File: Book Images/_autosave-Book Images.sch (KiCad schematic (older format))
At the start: 5 parts, among them T1 Transformer

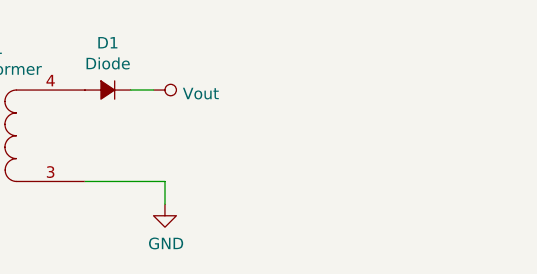
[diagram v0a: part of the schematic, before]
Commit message: adding images and rewriting intro
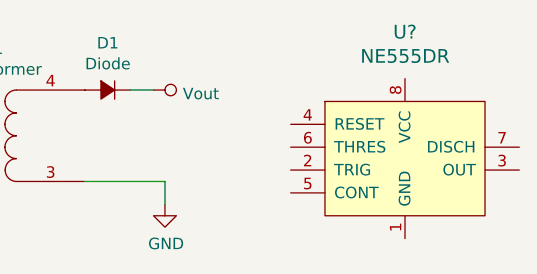
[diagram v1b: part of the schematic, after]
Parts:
- added U?: NE555DR, digikey-footprints:SOIC-8_W3.9mm, symbol dk_Clock-Timing-Programmable-Timers-and-Oscillators:NE555DR
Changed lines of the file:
@@
 Wire Wire Line
 	3350 2600 3000 2600
+$Comp
+L dk_Clock-Timing-Programmable-Timers-and-Oscillators:NE555DR U?
+U 1 1 624B1200
+P 4400 2250
+F 0 "U?" H 4400 2553 60  0000 C CNN
+F 1 "NE555DR" H 4400 2447 60  0000 C CNN
+F 2 "digikey-footprints:SOIC-8_W3.9mm" H 4600 2450 60  0001 L CNN
+F 3 "http://www.ti.com/general/docs/suppproductinfo.tsp?distId=10&gotoUrl=http%3A%2F%2Fwww.ti.com%2Flit%2Fgpn%2Fne555" H 4600 2550 60  0001 L CNN
+F 4 "296-6501-1-ND" H 4600 2650 60  0001 L CNN "Digi-Key_PN"
+F 5 "NE555DR" H 4600 2750 60  0001 L CNN "MPN"
+F 6 "Integrated Circuits (ICs)" H 4600 2850 60  0001 L CNN "Category"
+F 7 "Clock/Timing - Programmable Timers and Oscillators" H 4600 2950 60  0001 L CNN "Family"
+F 8 "http://www.ti.com/general/docs/suppproductinfo.tsp?distId=10&gotoUrl=http%3A%2F%2Fwww.ti.com%2Flit%2Fgpn%2Fne555" H 4600 3050 60  0001 L CNN "DK_Datasheet_Link"
+F 9 "/product-detail/en/texas-instruments/NE555DR/296-6501-1-ND/372490" H 4600 3150 60  0001 L CNN "DK_Detail_Page"
+F 10 "IC OSC SGL TIMER 100KHZ 8-SOIC" H 4600 3250 60  0001 L CNN "Description"
+F 11 "Texas Instruments" H 4600 3350 60  0001 L CNN "Manufacturer"
+F 12 "Active" H 4600 3450 60  0001 L CNN "Status"
+	1    4400 2250
+	1    0    0    -1
+$EndComp
 $EndSCHEMATC

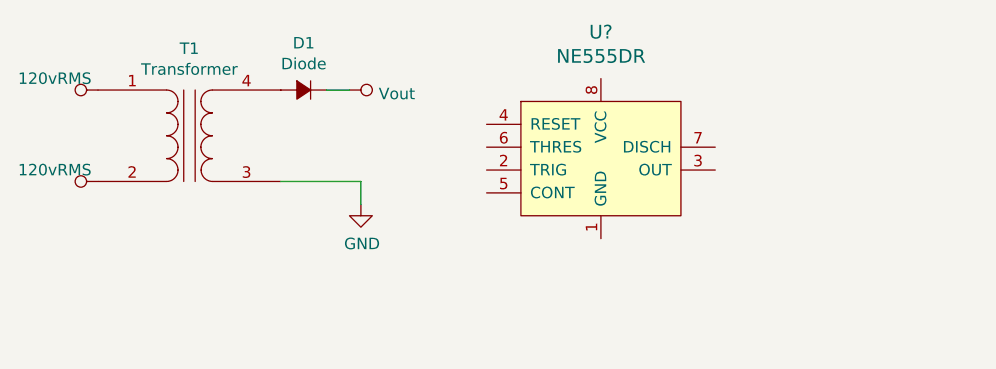
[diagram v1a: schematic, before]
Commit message: updated formating and added unregulated section
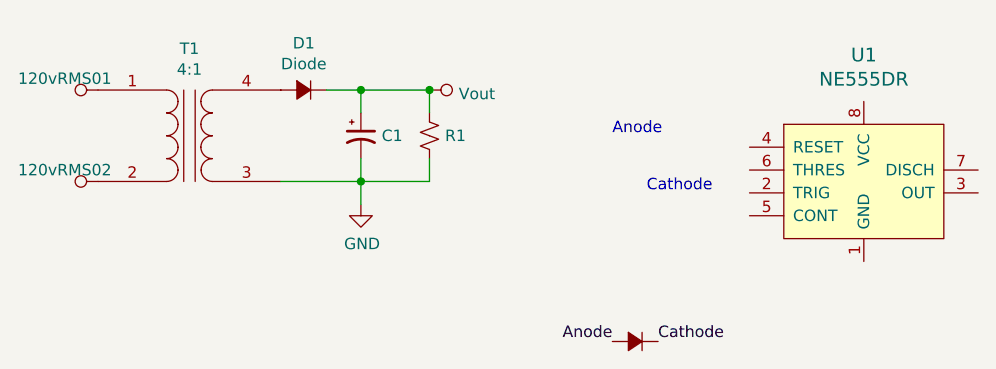
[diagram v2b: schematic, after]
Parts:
- added C1: CP1_Small, symbol Device:CP1_Small
- added D2: Diode, symbol Device:D_Small_ALT
- added R1: R_Small_US, symbol Device:R_Small_US
- T1: value Transformer -> 4:1
- gave numbers to parts that had none: 1
- renumbered 120vRMS to 120vRMS01, 120vRMS to 120vRMS02
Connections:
- net GND: now also C1.2, R1.2
- net LINE: now also C1.1, R1.1
- new net Anode: D2.2 (A)
- new net Cathode: D2.1 (K)
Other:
- note added: "Anode"
- note added: "Cathode"
- moved on the sheet: U1
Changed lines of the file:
@@
 P 2600 2400
 F 0 "T1" H 2600 2781 50  0000 C CNN
-F 1 "Transformer" H 2600 2690 50  0000 C CNN
+F 1 "4:1" H 2600 2690 50  0000 C CNN
 F 2 "" H 2600 2400 50  0001 C CNN
 F 3 "~" H 2600 2400 50  0001 C CNN
 	1    2600 2400
 	1    0    0    -1
-$EndComp
-$Comp
-L Device:D_Small_ALT D1
-U 1 1 62476573
-P 3100 2200
-F 0 "D1" H 3100 1995 50  0000 C CNN
-F 1 "Diode" H 3100 2086 50  0000 C CNN
-F 2 "" V 3100 2200 50  0001 C CNN
-F 3 "~" V 3100 2200 50  0001 C CNN
-	1    3100 2200
-	-1   0    0    1
 $EndComp
 $Comp
@@
 L power:LINE Vout
 U 1 1 624789B6
-P 3300 2200
-F 0 "Vout" V 3317 2328 50  0000 L CNN
-F 1 "LINE" V 3317 2328 50  0001 L CNN
-F 2 "" H 3300 2200 50  0001 C CNN
-F 3 "" H 3300 2200 50  0001 C CNN
-	1    3300 2200
+P 3650 2200
+F 0 "Vout" V 3667 2328 50  0000 L CNN
+F 1 "LINE" V 3667 2328 50  0001 L CNN
+F 2 "" H 3650 2200 50  0001 C CNN
+F 3 "" H 3650 2200 50  0001 C CNN
+	1    3650 2200
 	0    1    1    0
 $EndComp
-Wire Wire Line
-	3300 2200 3200 2200
 $Comp
-L power:LINE 120vRMS
+L power:LINE 120vRMS01
 U 1 1 62479B19
 P 2200 2200
-F 0 "120vRMS" V 2250 2550 50  0000 R CNN
+F 0 "120vRMS01" V 2250 2550 50  0000 R CNN
 F 1 "LINE" V 2217 2328 50  0001 L CNN
 F 2 "" H 2200 2200 50  0001 C CNN
@@
 $EndComp
 $Comp
-L power:LINE 120vRMS
+L power:LINE 120vRMS02
 U 1 1 6247B017
 P 2200 2600
-F 0 "120vRMS" V 2250 2950 50  0000 R CNN
+F 0 "120vRMS02" V 2250 2950 50  0000 R CNN
 F 1 "LINE" V 2217 2728 50  0001 L CNN
 F 2 "" H 2200 2600 50  0001 C CNN
@@
 	3350 2600 3000 2600
 $Comp
-L dk_Clock-Timing-Programmable-Timers-and-Oscillators:NE555DR U?
+L dk_Clock-Timing-Programmable-Timers-and-Oscillators:NE555DR U1
 U 1 1 624B1200
-P 4400 2250
-F 0 "U?" H 4400 2553 60  0000 C CNN
-F 1 "NE555DR" H 4400 2447 60  0000 C CNN
-F 2 "digikey-footprints:SOIC-8_W3.9mm" H 4600 2450 60  0001 L CNN
-F 3 "http://www.ti.com/general/docs/suppproductinfo.tsp?distId=10&gotoUrl=http%3A%2F%2Fwww.ti.com%2Flit%2Fgpn%2Fne555" H 4600 2550 60  0001 L CNN
-F 4 "296-6501-1-ND" H 4600 2650 60  0001 L CNN "Digi-Key_PN"
-F 5 "NE555DR" H 4600 2750 60  0001 L CNN "MPN"
-F 6 "Integrated Circuits (ICs)" H 4600 2850 60  0001 L CNN "Category"
-F 7 "Clock/Timing - Programmable Timers and Oscillators" H 4600 2950 60  0001 L CNN "Family"
-F 8 "http://www.ti.com/general/docs/suppproductinfo.tsp?distId=10&gotoUrl=http%3A%2F%2Fwww.ti.com%2Flit%2Fgpn%2Fne555" H 4600 3050 60  0001 L CNN "DK_Datasheet_Link"
-F 9 "/product-detail/en/texas-instruments/NE555DR/296-6501-1-ND/372490" H 4600 3150 60  0001 L CNN "DK_Detail_Page"
-F 10 "IC OSC SGL TIMER 100KHZ 8-SOIC" H 4600 3250 60  0001 L CNN "Description"
-F 11 "Texas Instruments" H 4600 3350 60  0001 L CNN "Manufacturer"
-F 12 "Active" H 4600 3450 60  0001 L CNN "Status"
-	1    4400 2250
+P 5550 2350
+F 0 "U1" H 5550 2653 60  0000 C CNN
+F 1 "NE555DR" H 5550 2547 60  0000 C CNN
+F 2 "digikey-footprints:SOIC-8_W3.9mm" H 5750 2550 60  0001 L CNN
+F 3 "http://www.ti.com/general/docs/suppproductinfo.tsp?distId=10&gotoUrl=http%3A%2F%2Fwww.ti.com%2Flit%2Fgpn%2Fne555" H 5750 2650 60  0001 L CNN
+F 4 "296-6501-1-ND" H 5750 2750 60  0001 L CNN "Digi-Key_PN"
+F 5 "NE555DR" H 5750 2850 60  0001 L CNN "MPN"
+F 6 "Integrated Circuits (ICs)" H 5750 2950 60  0001 L CNN "Category"
+F 7 "Clock/Timing - Programmable Timers and Oscillators" H 5750 3050 60  0001 L CNN "Family"
+F 8 "http://www.ti.com/general/docs/suppproductinfo.tsp?distId=10&gotoUrl=http%3A%2F%2Fwww.ti.com%2Flit%2Fgpn%2Fne555" H 5750 3150 60  0001 L CNN "DK_Datasheet_Link"
+F 9 "/product-detail/en/texas-instruments/NE555DR/296-6501-1-ND/372490" H 5750 3250 60  0001 L CNN "DK_Detail_Page"
+F 10 "IC OSC SGL TIMER 100KHZ 8-SOIC" H 5750 3350 60  0001 L CNN "Description"
+F 11 "Texas Instruments" H 5750 3450 60  0001 L CNN "Manufacturer"
+F 12 "Active" H 5750 3550 60  0001 L CNN "Status"
+	1    5550 2350
 	1    0    0    -1
 $EndComp
+Text Notes 4450 2400 0    50   ~ 0
+Anode
+$Comp
+L Device:D_Small_ALT D1
+U 1 1 62476573
+P 3100 2200
+F 0 "D1" H 3100 1995 50  0000 C CNN
+F 1 "Diode" H 3100 2086 50  0000 C CNN
+F 2 "" V 3100 2200 50  0001 C CNN
+F 3 "~" V 3100 2200 50  0001 C CNN
+	1    3100 2200
+	-1   0    0    1
+$EndComp
+$Comp
+L Device:D_Small_ALT D2
+U 1 1 62795DA9
+P 4550 3300
+F 0 "D2" H 4550 3095 50  0001 C CNN
+F 1 "Diode" H 4550 3186 50  0001 C CNN
+F 2 "" V 4550 3300 50  0001 C CNN
+F 3 "~" V 4550 3300 50  0001 C CNN
+	1    4550 3300
+	-1   0    0    1
+$EndComp
+Text Notes 4600 2650 0    50   ~ 0
+Cathode
+Text Label 4450 3300 2    50   ~ 0
+Anode
+Text Label 4650 3300 0    50   ~ 0
+Cathode
+$Comp
+L Device:CP1_Small C1
+U 1 1 6279770B
+P 3350 2400
+F 0 "C1" H 3441 2400 50  0000 L CNN
+F 1 "CP1_Small" H 3441 2355 50  0001 L CNN
+F 2 "" H 3350 2400 50  0001 C CNN
+F 3 "~" H 3350 2400 50  0001 C CNN
+	1    3350 2400
+	1    0    0    -1
+$EndComp
+Wire Wire Line
+	3350 2300 3350 2200
+Wire Wire Line
+	3200 2200 3350 2200
+Wire Wire Line
+	3350 2500 3350 2600
+Connection ~ 3350 2600
+$Comp
+L Device:R_Small_US R1
+U 1 1 62799E07
+P 3650 2400
+F 0 "R1" H 3718 2400 50  0000 L CNN
+F 1 "R_Small_US" H 3718 2355 50  0001 L CNN
+F 2 "" H 3650 2400 50  0001 C CNN
+F 3 "~" H 3650 2400 50  0001 C CNN
+	1    3650 2400
+	1    0    0    -1
+$EndComp
+Wire Wire Line
+	3650 2500 3650 2600
+Wire Wire Line
+	3650 2600 3350 2600
+Wire Wire Line
+	3650 2300 3650 2200
+Wire Wire Line
+	3650 2200 3350 2200
+Connection ~ 3350 2200
+Connection ~ 3650 2200
 $EndSCHEMATC

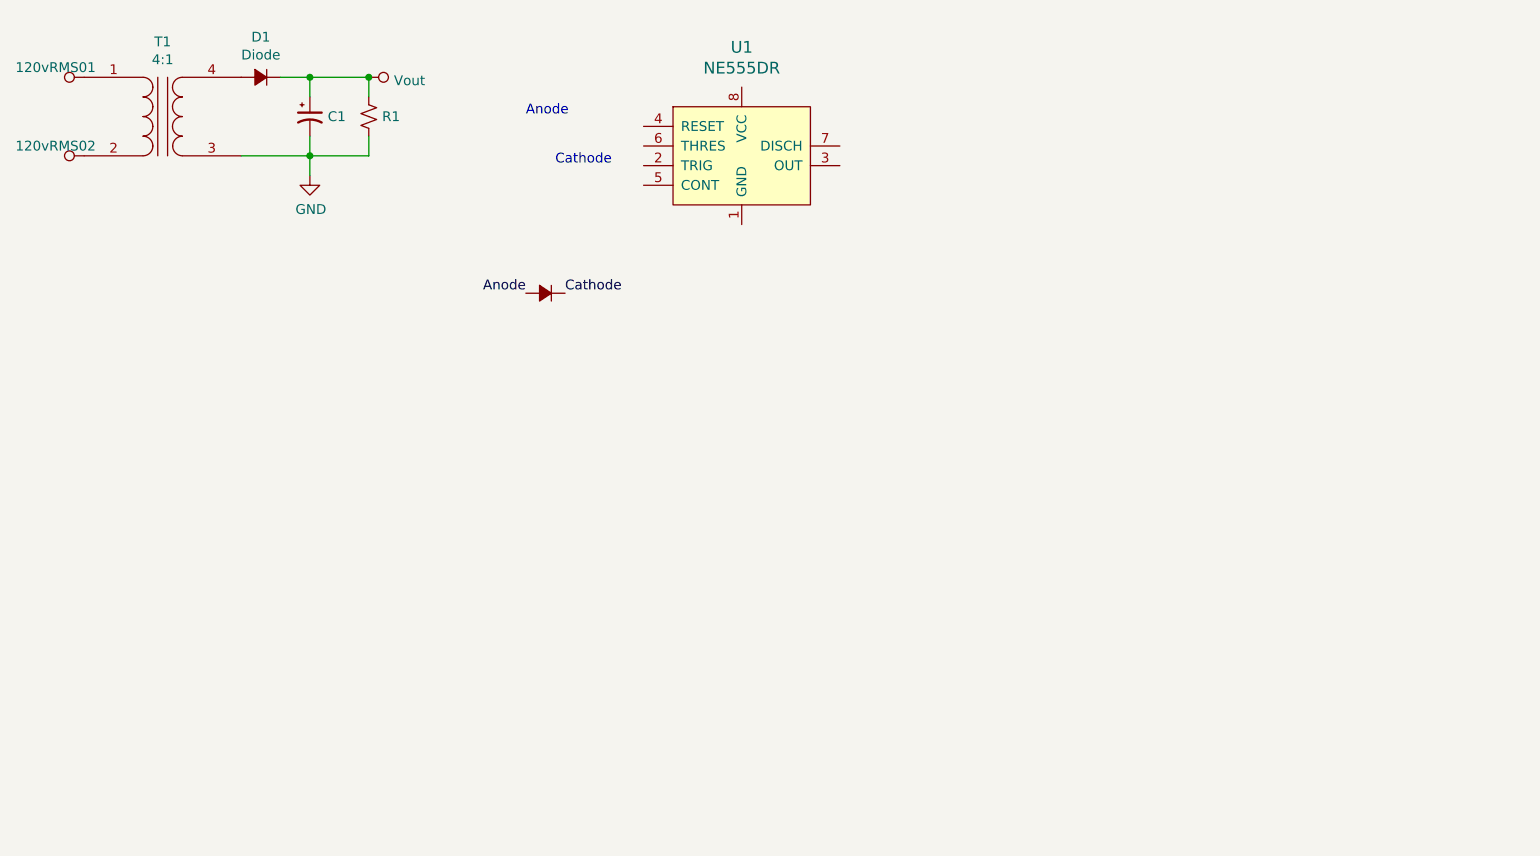
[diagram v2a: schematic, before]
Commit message: finished basic regulation
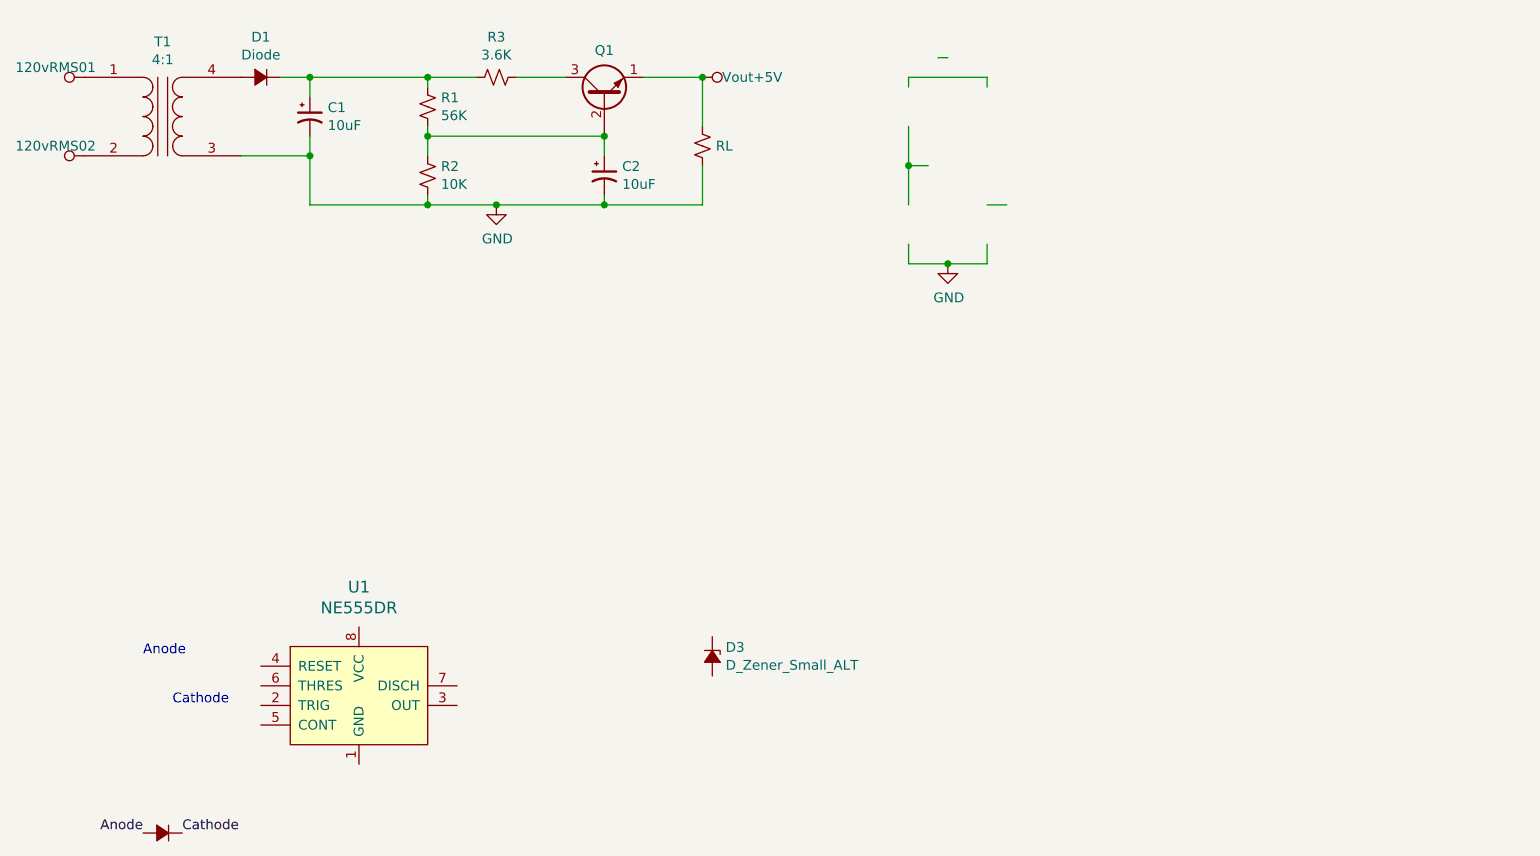
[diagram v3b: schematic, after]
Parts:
- added C2: 10uF, symbol Device:CP1_Small
- added D3: D_Zener_Small_ALT, symbol Device:D_Zener_Small_ALT
- added Q1: 2N3904, Package_TO_SOT_THT:TO-92_Inline, symbol Transistor_BJT:2N3904
- added R2: 10K, symbol Device:R_Small_US
- added R3: 3.6K, symbol Device:R_Small_US
- added RL: R_Small_US, symbol Device:R_Small_US
- C1: value CP1_Small -> 10uF
- R1: value R_Small_US -> 56K
- renumbered Vout to Vout+5V
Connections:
- wire segments 9 -> 34
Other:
- moved on the sheet: U1

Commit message: finished BJT regulators starting 7805
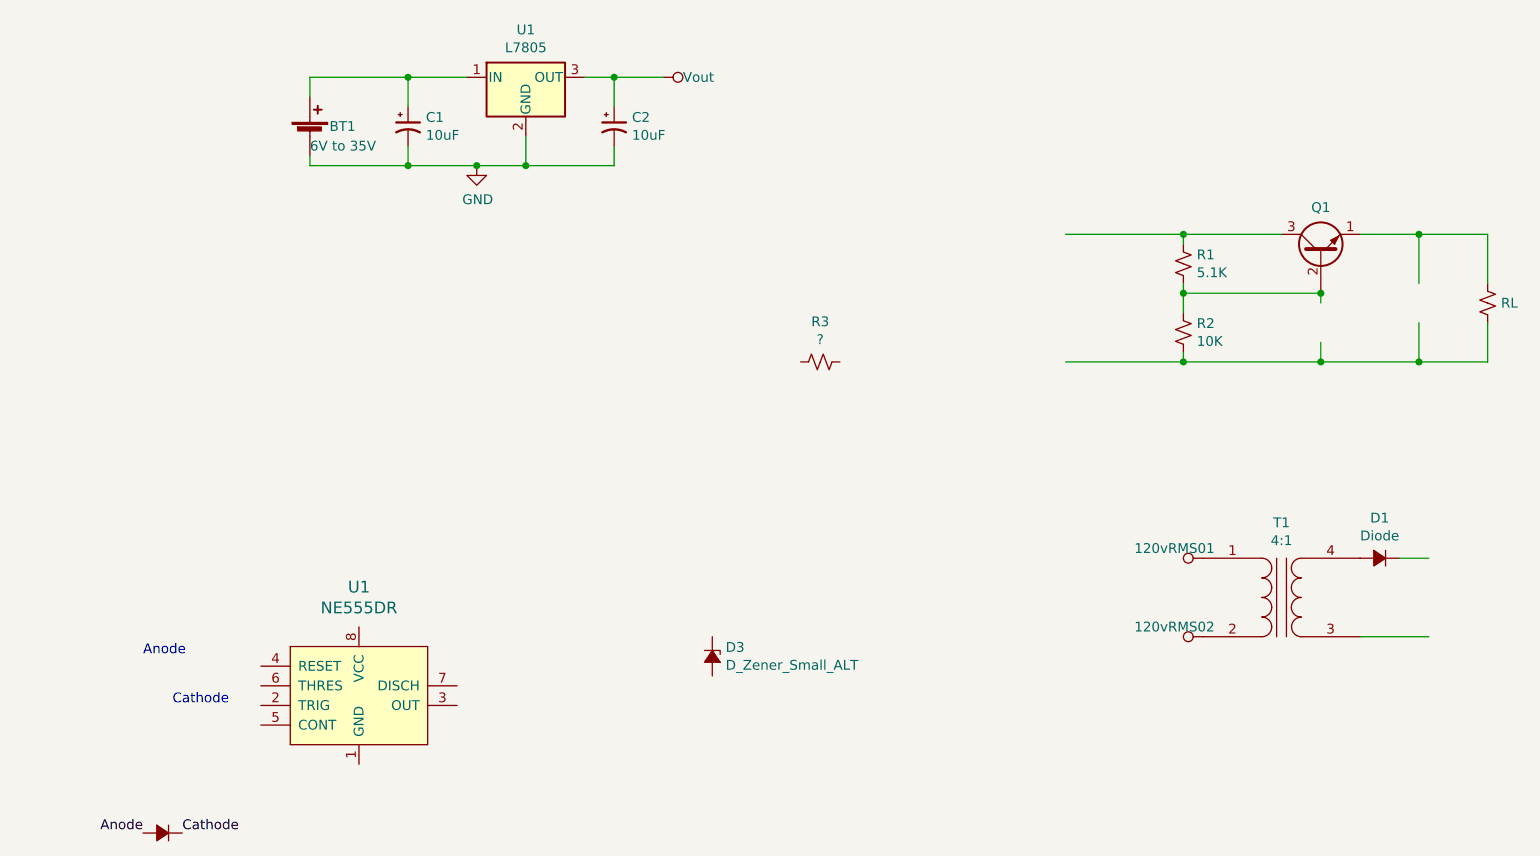
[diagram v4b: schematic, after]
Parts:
- added BT1: 6V to 35V, symbol Device:Battery_Cell
- added U1: L7805, symbol Regulator_Linear:L7805
- R1: value 56K -> 5.1K
- R3: value 3.6K -> ?
- renumbered Vout+5V to Vout
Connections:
- wire segments 34 -> 36
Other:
- moved on the sheet: C1, C2, D1, Q1, R1, R2, R3, RL, T1
